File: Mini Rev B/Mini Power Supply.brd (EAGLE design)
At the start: 68.6 x 31.8 mm, 29 parts

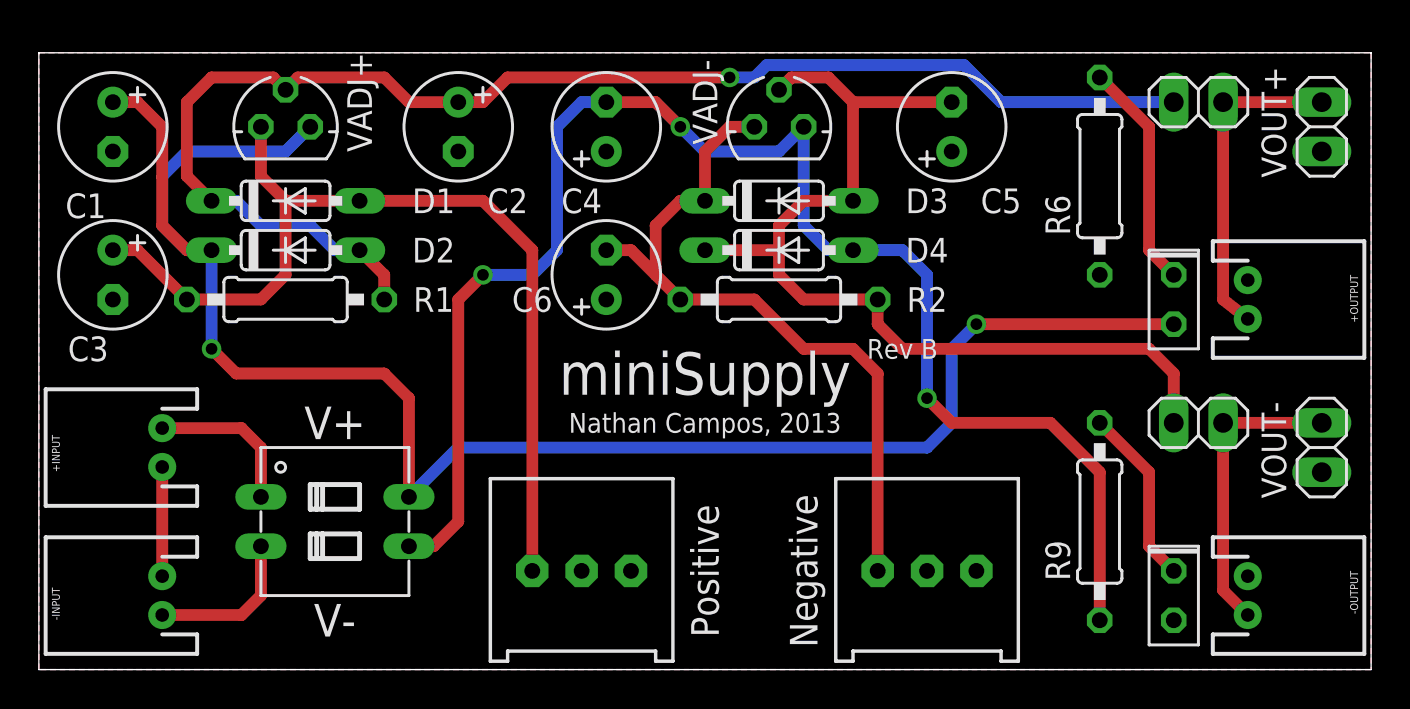
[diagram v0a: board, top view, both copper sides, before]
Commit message: Fixed the negative voltage regulator
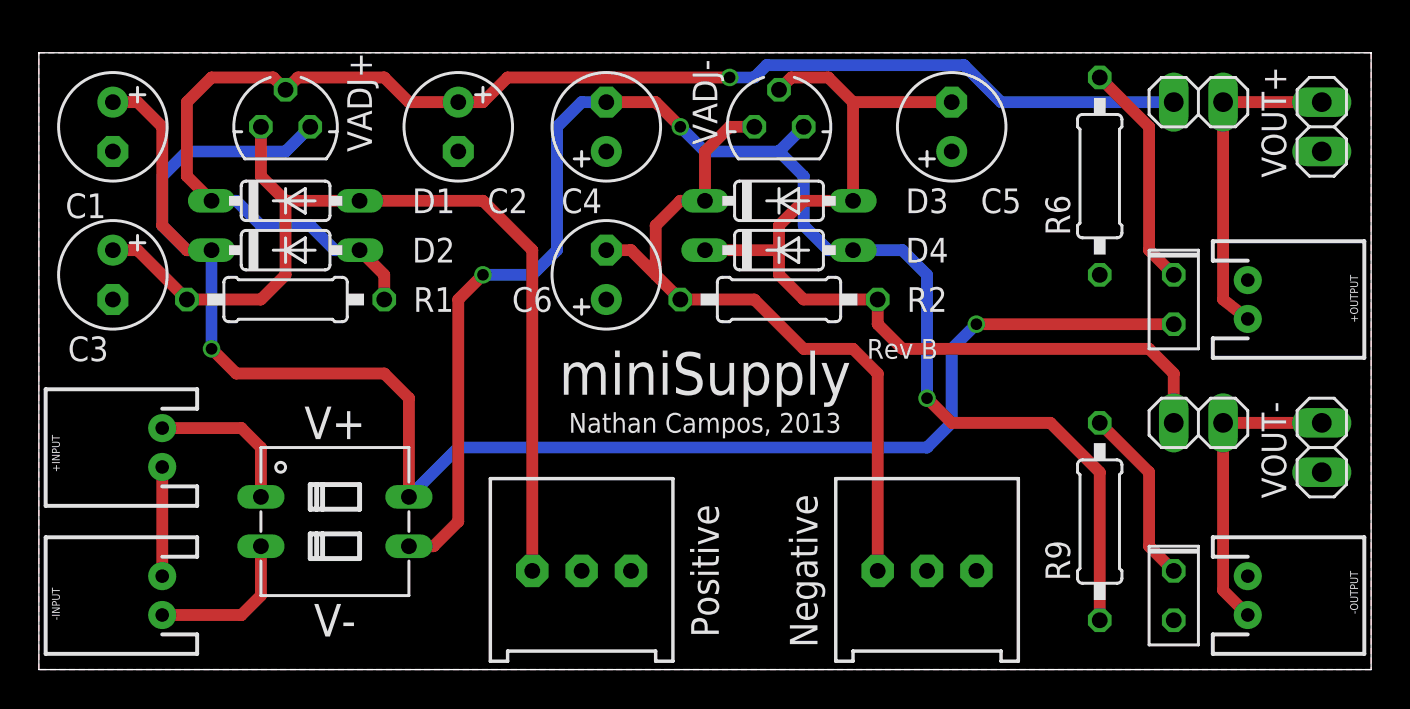
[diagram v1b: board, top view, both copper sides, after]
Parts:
- VADJ-: device v-reg:317L -> v-reg:337L
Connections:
- net -VOUT: now also VADJ-.OUT; no longer VADJ-.2
- net N$1: now also VADJ-.ADJ; no longer VADJ-.1
- net V-: now also VADJ-.IN; no longer VADJ-.3
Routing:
- net V-: track 78.7 -> 78.0 mm
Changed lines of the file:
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@@
 <layers>
 <layer number="1" name="Top" color="4" fill="1" visible="yes" active="yes"/>
-<layer number="2" name="Route2" color="1" fill="3" visible="no" active="no"/>
+<layer number="2" name="Route2" color="1" fill="3" visible="no" active="yes"/>
 <layer number="3" name="Route3" color="4" fill="3" visible="no" active="no"/>
 <layer number="14" name="Route14" color="1" fill="6" visible="no" active="no"/>
-<layer number="15" name="Route15" color="4" fill="6" visible="no" active="no"/>
+<layer number="15" name="Route15" color="4" fill="6" visible="yes" active="yes"/>
 <layer number="16" name="Bottom" color="1" fill="1" visible="yes" active="yes"/>
 <layer number="17" name="Pads" color="2" fill="1" visible="yes" active="yes"/>
@@
 </class>
 </classes>
-<designrules name="default">
+<designrules name="SeeedStudio_DRU_no_angle_20130527">
 <description language="de">&lt;b&gt;EAGLE Design Rules&lt;/b&gt;
 &lt;p&gt;
@@
 necessary adjustments and save your customized
 design rules under a new name.</description>
-<param name="layerSetup" value="(1*16)"/>
-<param name="mtCopper" value="0.035mm 0.035mm 0.035mm 0.035mm 0.035mm 0.035mm 0.035mm 0.035mm 0.035mm 0.035mm 0.035mm 0.035mm 0.035mm 0.035mm 0.035mm 0.035mm"/>
-<param name="mtIsolate" value="1.5mm 0.15mm 0.2mm 0.15mm 0.2mm 0.15mm 0.2mm 0.15mm 0.2mm 0.15mm 0.2mm 0.15mm 0.2mm 0.15mm 0.2mm"/>
-<param name="mdWireWire" value="8mil"/>
-<param name="mdWirePad" value="8mil"/>
-<param name="mdWireVia" value="8mil"/>
-<param name="mdPadPad" value="8mil"/>
-<param name="mdPadVia" value="8mil"/>
-<param name="mdViaVia" value="8mil"/>
-<param name="mdSmdPad" value="8mil"/>
-<param name="mdSmdVia" value="8mil"/>
-<param name="mdSmdSmd" value="8mil"/>
+<description language="zh">&lt;b&gt;Seeed Studio EAGLE Design Rules&lt;/b&gt;
+</description>
+<param name="layerSetup" value="(1*2*15*16)"/>
+<param name="mtCopper" value="0.035mm 0.0175mm 0.035mm 0.035mm 0.035mm 0.035mm 0.035mm 0.035mm 0.035mm 0.035mm 0.035mm 0.035mm 0.035mm 0.035mm 0.0175mm 0.035mm"/>
+<param name="mtIsolate" value="0.2mm 1.1mm 0.2mm 0.15mm 0.2mm 0.15mm 0.2mm 0.15mm 0.2mm 0.15mm 0.2mm 0.15mm 0.2mm 0.15mm 0.2mm"/>
+<param name="mdWireWire" value="6mil"/>
+<param name="mdWirePad" value="6mil"/>
+<param name="mdWireVia" value="6mil"/>
+<param name="mdPadPad" value="6mil"/>
+<param name="mdPadVia" value="6mil"/>
+<param name="mdViaVia" value="6mil"/>
+<param name="mdSmdPad" value="0mil"/>
+<param name="mdSmdVia" value="0mil"/>
+<param name="mdSmdSmd" value="0mil"/>
 <param name="mdViaViaSameLayer" value="8mil"/>
 <param name="mnLayersViaInSmd" value="2"/>
-<param name="mdCopperDimension" value="40mil"/>
-<param name="mdDrill" value="8mil"/>
+<param name="mdCopperDimension" value="10mil"/>
+<param name="mdDrill" value="10mil"/>
 <param name="mdSmdStop" value="0mil"/>
-<param name="msWidth" value="10mil"/>
-<param name="msDrill" value="24mil"/>
-<param name="msMicroVia" value="9.99mm"/>
+<param name="msWidth" value="6mil"/>
+<param name="msDrill" value="12mil"/>
+<param name="msMicroVia" value="12mil"/>
 <param name="msBlindViaRatio" value="0.5"/>
 <param name="rvPadTop" value="0.25"/>
@@
 <param name="rvMicroViaOuter" value="0.25"/>
 <param name="rvMicroViaInner" value="0.25"/>
-<param name="rlMinPadTop" value="10mil"/>
+<param name="rlMinPadTop" value="6mil"/>
 <param name="rlMaxPadTop" value="20mil"/>
-<param name="rlMinPadInner" value="10mil"/>
+<param name="rlMinPadInner" value="6mil"/>
 <param name="rlMaxPadInner" value="20mil"/>
-<param name="rlMinPadBottom" value="10mil"/>
+<param name="rlMinPadBottom" value="6mil"/>
 <param name="rlMaxPadBottom" value="20mil"/>
-<param name="rlMinViaOuter" value="8mil"/>
+<param name="rlMinViaOuter" value="6mil"/>
 <param name="rlMaxViaOuter" value="20mil"/>
-<param name="rlMinViaInner" value="8mil"/>
+<param name="rlMinViaInner" value="6mil"/>
 <param name="rlMaxViaInner" value="20mil"/>
 <param name="rlMinMicroViaOuter" value="4mil"/>
@@
 <param name="psTop" value="-1"/>
 <param name="psBottom" value="-1"/>
-<param name="psFirst" value="-1"/>
+<param name="psFirst" value="0"/>
 <param name="psElongationLong" value="100"/>
 <param name="psElongationOffset" value="100"/>
 <param name="mvStopFrame" value="1"/>
 <param name="mvCreamFrame" value="0"/>
-<param name="mlMinStopFrame" value="4mil"/>
-<param name="mlMaxStopFrame" value="4mil"/>
+<param name="mlMinStopFrame" value="2mil"/>
+<param name="mlMaxStopFrame" value="2mil"/>
 <param name="mlMinCreamFrame" value="0mil"/>
 <param name="mlMaxCreamFrame" value="0mil"/>
-<param name="mlViaStopLimit" value="0mil"/>
+<param name="mlViaStopLimit" value="25mil"/>
 <param name="srRoundness" value="0"/>
 <param name="srMinRoundness" value="0mil"/>
@@
 <param name="checkAngle" value="0"/>
 <param name="checkFont" value="1"/>
-<param name="checkRestrict" value="1"/>
+<param name="checkRestrict" value="0"/>
 <param name="useDiameter" value="13"/>
 <param name="maxErrors" value="50"/>
@@
 <attribute name="VALUE" x="15.875" y="26.67" size="1.27" layer="27" ratio="10"/>
 </element>
-<element name="VADJ-" library="v-reg" package="317L" value="" x="38.1" y="27.94" smashed="yes">
+<element name="VADJ-" library="v-reg" package="337L" value="" x="38.1" y="27.94" smashed="yes">
 <attribute name="NAME" x="34.29" y="29.21" size="1.27" layer="25" ratio="10" rot="R90" align="center"/>
 <attribute name="VALUE" x="41.275" y="26.67" size="1.27" layer="27" ratio="10"/>
@@
 <contactref element="R2" pad="2"/>
 <contactref element="-I_PRB" pad="1"/>
-<contactref element="VADJ-" pad="2"/>
 <wire x1="41.91" y1="24.13" x2="41.91" y2="29.21" width="0.6096" layer="1"/>
 <wire x1="41.91" y1="29.21" x2="40.64" y2="30.48" width="0.6096" layer="1"/>
 <wire x1="40.64" y1="30.48" x2="38.735" y2="30.48" width="0.6096" layer="1"/>
-<wire x1="38.735" y1="30.48" x2="38.1" y2="29.845" width="0.6096" layer="1"/>
 <wire x1="43.18" y1="19.05" x2="39.37" y2="19.05" width="0.6096" layer="1"/>
 <wire x1="39.37" y1="19.05" x2="38.1" y2="20.32" width="0.6096" layer="1"/>
@@
 <wire x1="44.45" y1="16.51" x2="43.18" y2="17.78" width="0.6096" layer="1"/>
 <wire x1="43.18" y1="17.78" x2="43.18" y2="19.05" width="0.6096" layer="1"/>
+<contactref element="VADJ-" pad="OUT"/>
+<wire x1="38.735" y1="30.48" x2="38.1" y2="29.845" width="0.6096" layer="1"/>
 </signal>
 <signal name="N$3">
@@
 <contactref element="R2" pad="1"/>
 <contactref element="R4" pad="1"/>
-<contactref element="VADJ-" pad="1"/>
 <wire x1="34.29" y1="24.13" x2="34.29" y2="26.67" width="0.6096" layer="1"/>
 <wire x1="34.29" y1="26.67" x2="35.56" y2="27.94" width="0.6096" layer="1"/>
-<wire x1="35.56" y1="27.94" x2="36.83" y2="27.94" width="0.6096" layer="1"/>
 <wire x1="33.02" y1="19.05" x2="31.75" y2="20.32" width="0.6096" layer="1"/>
 <wire x1="31.75" y1="20.32" x2="31.75" y2="22.86" width="0.6096" layer="1"/>
@@
 <wire x1="39.37" y1="16.51" x2="36.83" y2="19.05" width="0.6096" layer="1"/>
 <wire x1="36.83" y1="19.05" x2="33.02" y2="19.05" width="0.6096" layer="1"/>
+<contactref element="VADJ-" pad="ADJ"/>
+<wire x1="35.56" y1="27.94" x2="36.83" y2="27.94" width="0.6096" layer="1"/>
 </signal>
 <signal name="N$2">
@@
 <contactref element="R9" pad="1"/>
 <contactref element="S1" pad="3"/>
-<contactref element="VADJ-" pad="3"/>
 <wire x1="41.91" y1="21.59" x2="40.64" y2="21.59" width="0.6096" layer="16"/>
 <wire x1="40.64" y1="21.59" x2="39.37" y2="22.86" width="0.6096" layer="16"/>
-<wire x1="39.37" y1="22.86" x2="39.37" y2="27.94" width="0.6096" layer="16"/>
 <wire x1="29.21" y1="29.21" x2="31.75" y2="29.21" width="0.6096" layer="1"/>
 <wire x1="31.75" y1="29.21" x2="33.02" y2="27.94" width="0.6096" layer="1"/>
@@
 <wire x1="33.02" y1="27.94" x2="34.29" y2="26.67" width="0.6096" layer="16"/>
 <wire x1="34.29" y1="26.67" x2="38.1" y2="26.67" width="0.6096" layer="16"/>
-<wire x1="38.1" y1="26.67" x2="39.37" y2="27.94" width="0.6096" layer="16"/>
 <wire x1="19.05" y1="6.35" x2="20.32" y2="6.35" width="0.6096" layer="1"/>
 <wire x1="20.32" y1="6.35" x2="21.59" y2="7.62" width="0.6096" layer="1"/>
@@
 <wire x1="44.45" y1="21.59" x2="45.72" y2="20.32" width="0.6096" layer="16"/>
 <wire x1="45.72" y1="20.32" x2="45.72" y2="13.97" width="0.6096" layer="16"/>
+<contactref element="VADJ-" pad="IN"/>
+<wire x1="38.1" y1="26.67" x2="39.37" y2="27.94" width="0.6096" layer="16"/>
+<wire x1="39.37" y1="22.86" x2="39.37" y2="25.4" width="0.6096" layer="16"/>
+<wire x1="39.37" y1="25.4" x2="38.1" y2="26.67" width="0.6096" layer="16"/>
 </signal>
 <signal name="+VOUT">
